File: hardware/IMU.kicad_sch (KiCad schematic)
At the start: 24 parts, among them IC2 LDFPVR, Q1 BSS138, Q2 BSS138, Q3 BSS138, Q4 BSS138, U4 ICM-20948

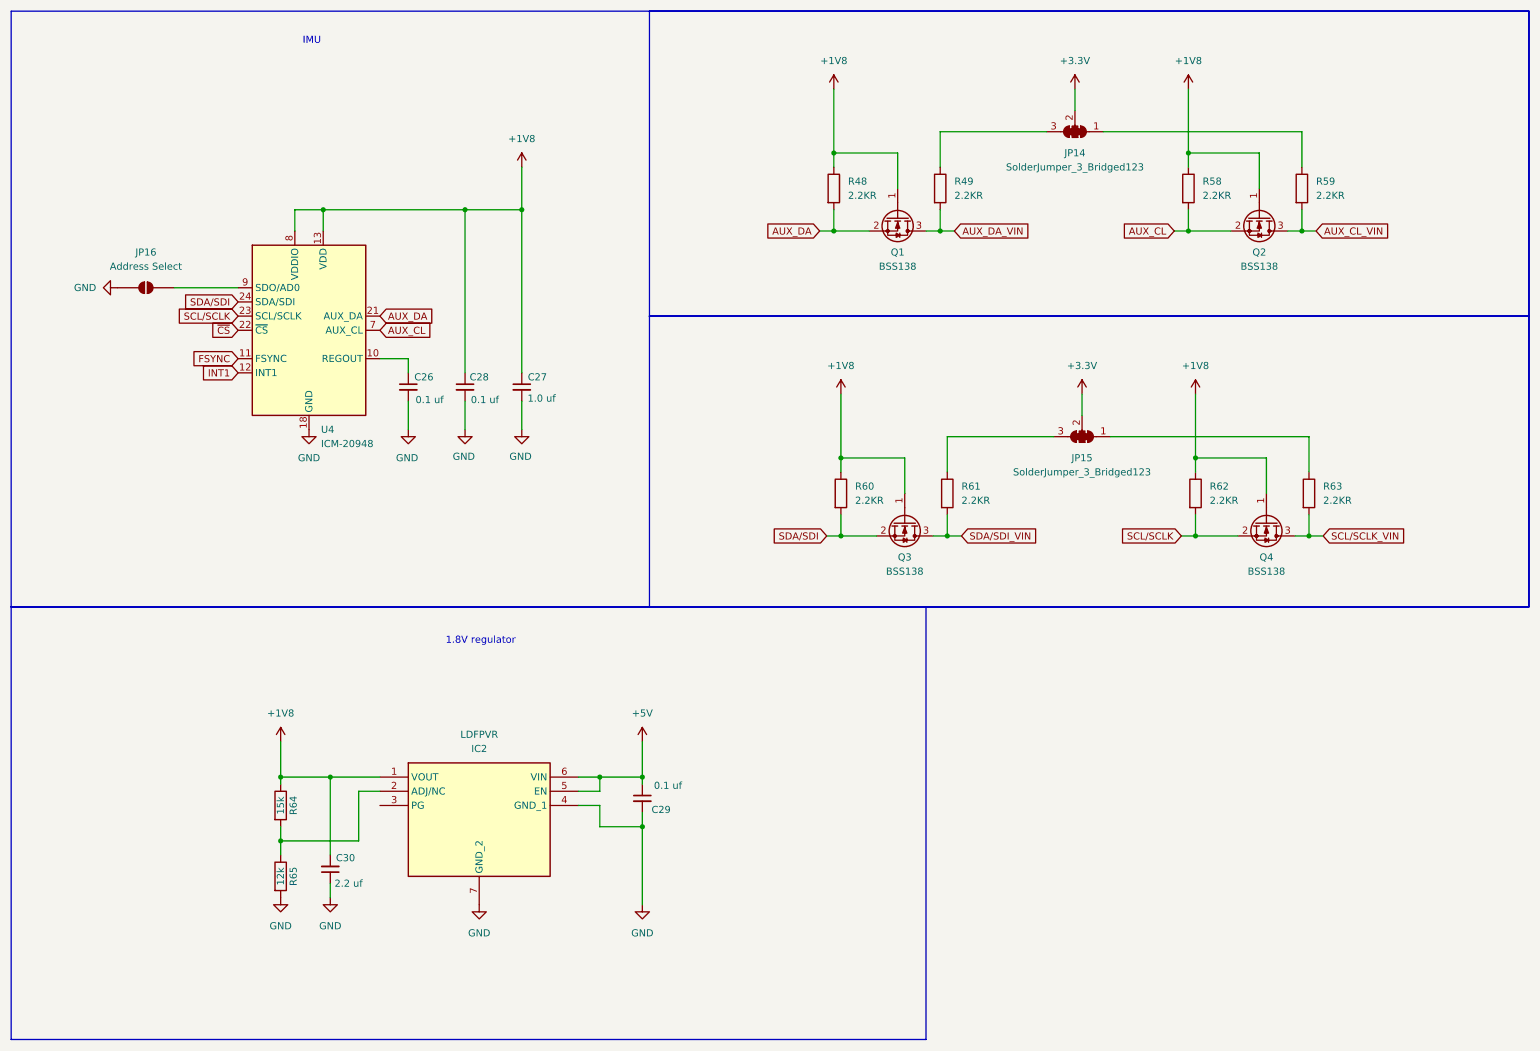
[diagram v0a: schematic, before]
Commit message: migrate to impart gui, begin redo of imu schematic
add to symbol library: ImpartGUI |
${KICAD_3RD_PARTY}/ImpartGUI.kicad_sym | format KiCad. add to footprint
library: ImpartGUI | ${KICAD_3RD_PARTY}/ImpartGUI.pretty | KiCad
-This is a choice made to keep project portable at the cost of larger
repo size.
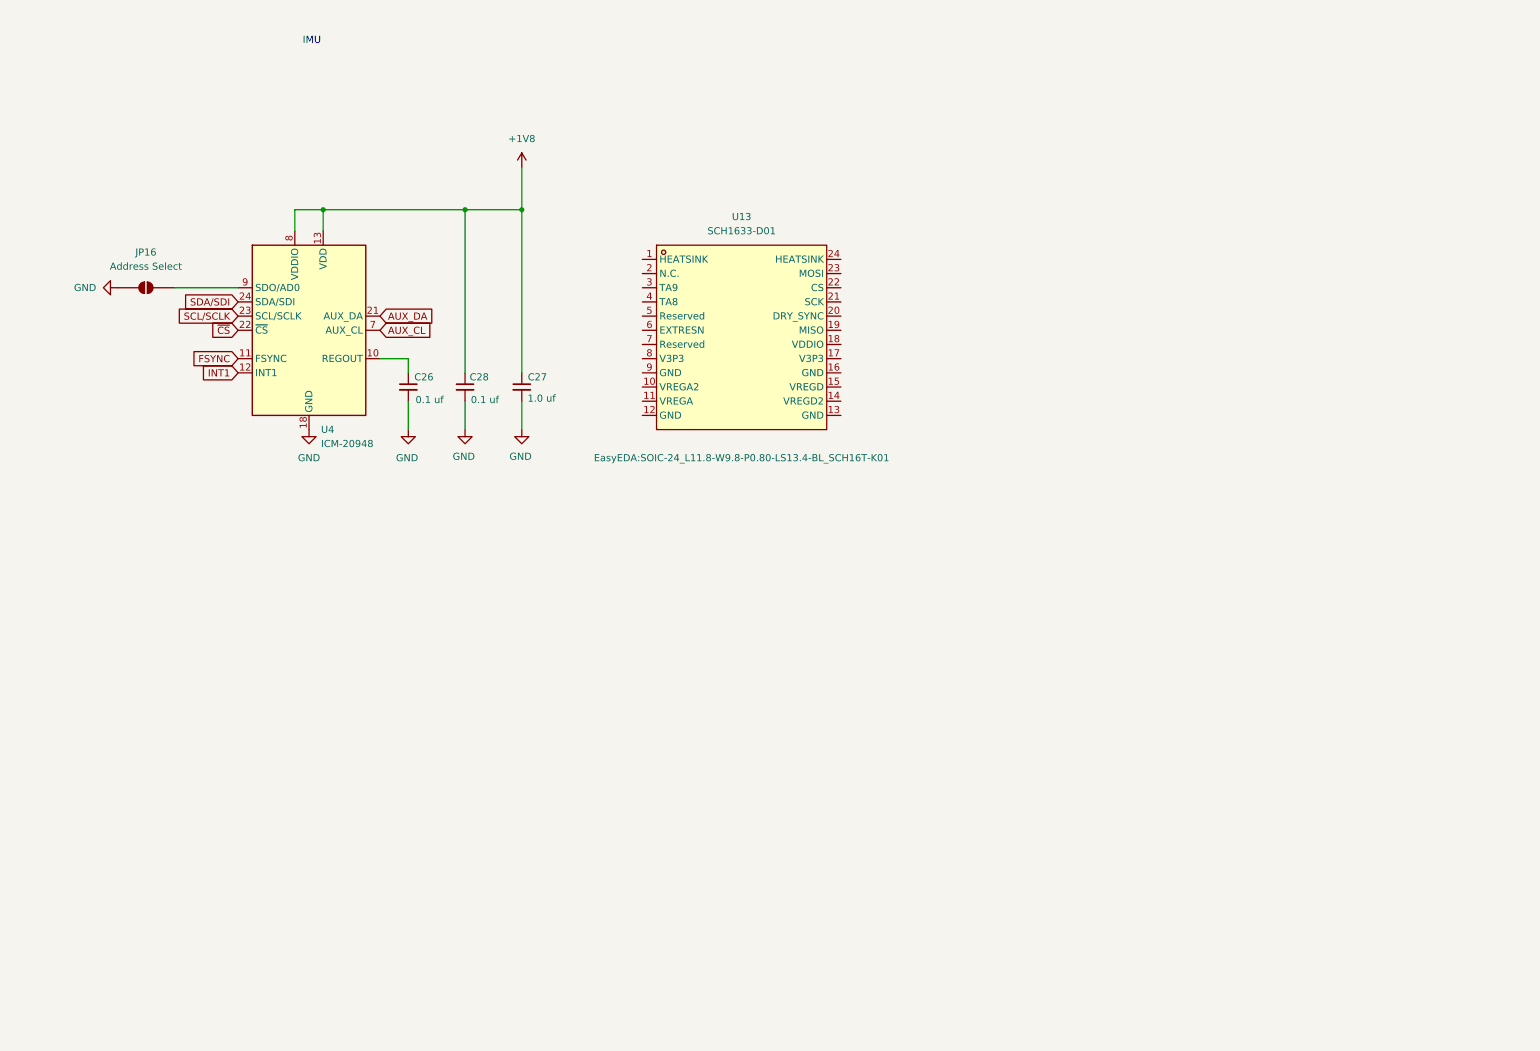
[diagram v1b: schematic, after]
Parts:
- removed C29: 0.1 uf, symbol Device:C_Small
- removed C30: 2.2 uf, symbol Device:C_Small
- removed IC2: LDFPVR, SON65P200X200X100-7N-D, symbol Loaded_Libraries:LDFPVR
- removed JP14, JP15: SolderJumper_3_Bridged123, symbol Jumper:SolderJumper_3_Bridged123
- removed Q1, Q2, Q3, Q4: BSS138, Package_TO_SOT_SMD:SOT-23, symbol Transistor_FET:BSS138
- removed R48, R49, R58, R59, R60, R61, R62, R63: 2.2KR, symbol Device:R
- removed R64: 15k, symbol Device:R
- removed R65: 12k, symbol Device:R
- added U13: SCH1633-D01, EasyEDA:SOIC-24_L11.8-W9.8-P0.80-LS13.4-BL_SCH16T-K01, symbol Lib_Loader:SCH1633-D01
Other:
- note removed: "1.8V regulator"
